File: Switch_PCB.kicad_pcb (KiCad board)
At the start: 2 copper layers, 213 x 96.6 mm, 75 parts, among them J1 Black, J10 Black, J11 Red, J12 Conn_01x02, J13 Conn_01x03, J14 Conn_01x03, J15 Conn_01x03, J16 Conn_01x03, J17 Jack 2.1mm, J18 Jack 2.1mm, J19 Black, J2 Red, J20 Red, J21 Black, J22 Red, J23 Black, J24 Red, J25 Black, J26 Red, J27 Black, J28 Red, J29 Black, J3 Black, J30 Red, J31 Black, J32 Red, J33 Black, J34 Red, J4 Red, J5 Black, J6 Red, J7 Black, J8 Red, J9 Red, SW1 Switch On-Off-On, SW2 Switch On-Off-On, SW3 Switch On-Off-On, SW4 Switch On-Off-On

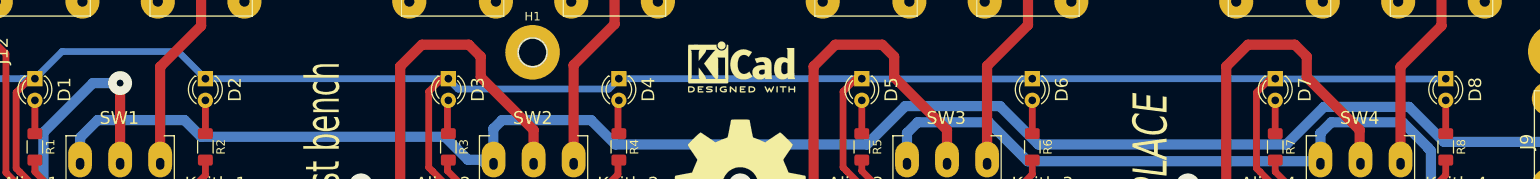
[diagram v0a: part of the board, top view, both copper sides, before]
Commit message: Change LED 3mm with 15.2mm Leads for 18 mm high * LED_D3.0mm_H18.0mm_Red * LED_D3.0mm_H18.0mm_Green
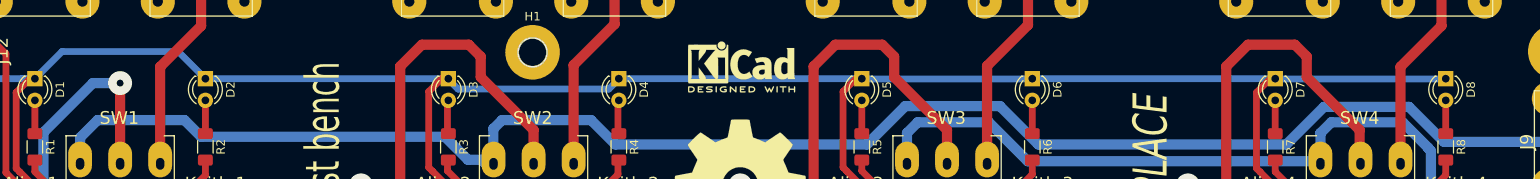
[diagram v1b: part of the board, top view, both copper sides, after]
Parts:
- D1, D3, D5, D7: footprint LED_THT:LED_D3.0mm -> Local_LED_THT:LED_D3.0mm_H18.0mm_Red
- D2, D4, D6, D8: footprint LED_THT:LED_D3.0mm -> Local_LED_THT:LED_D3.0mm_H18.0mm_Green

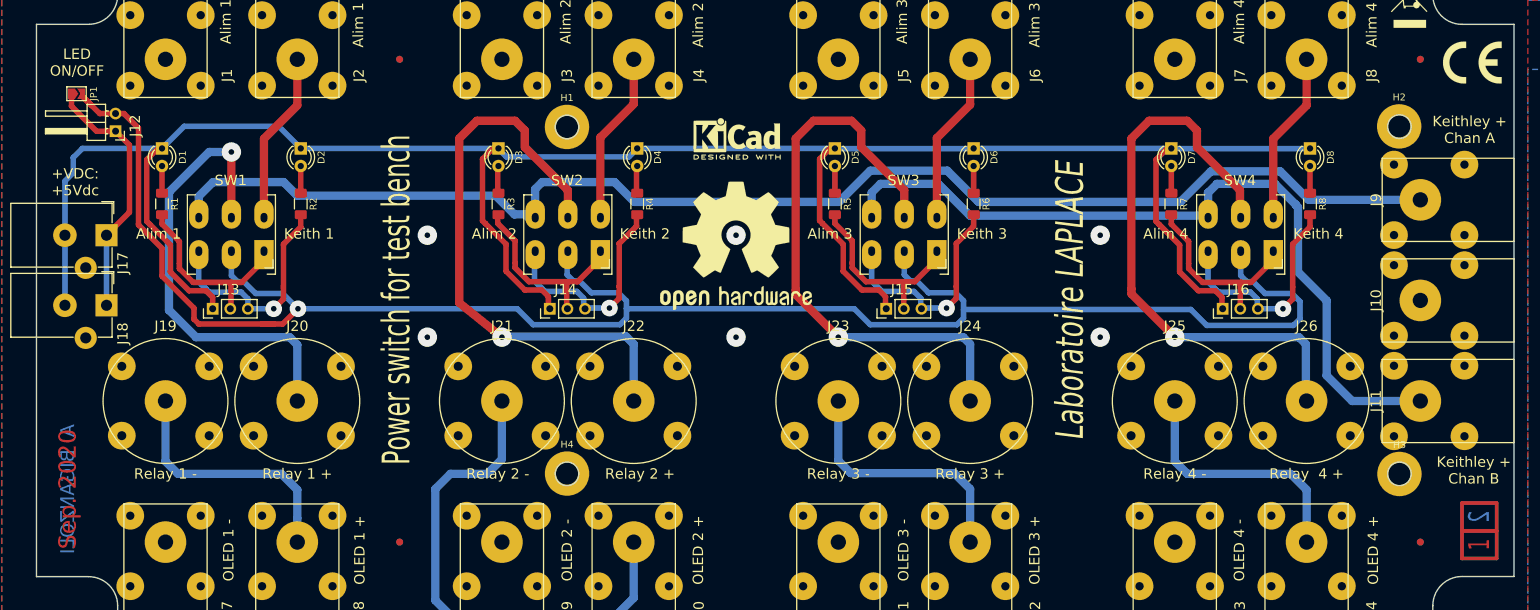
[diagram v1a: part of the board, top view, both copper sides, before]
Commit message: Update mechanical integration
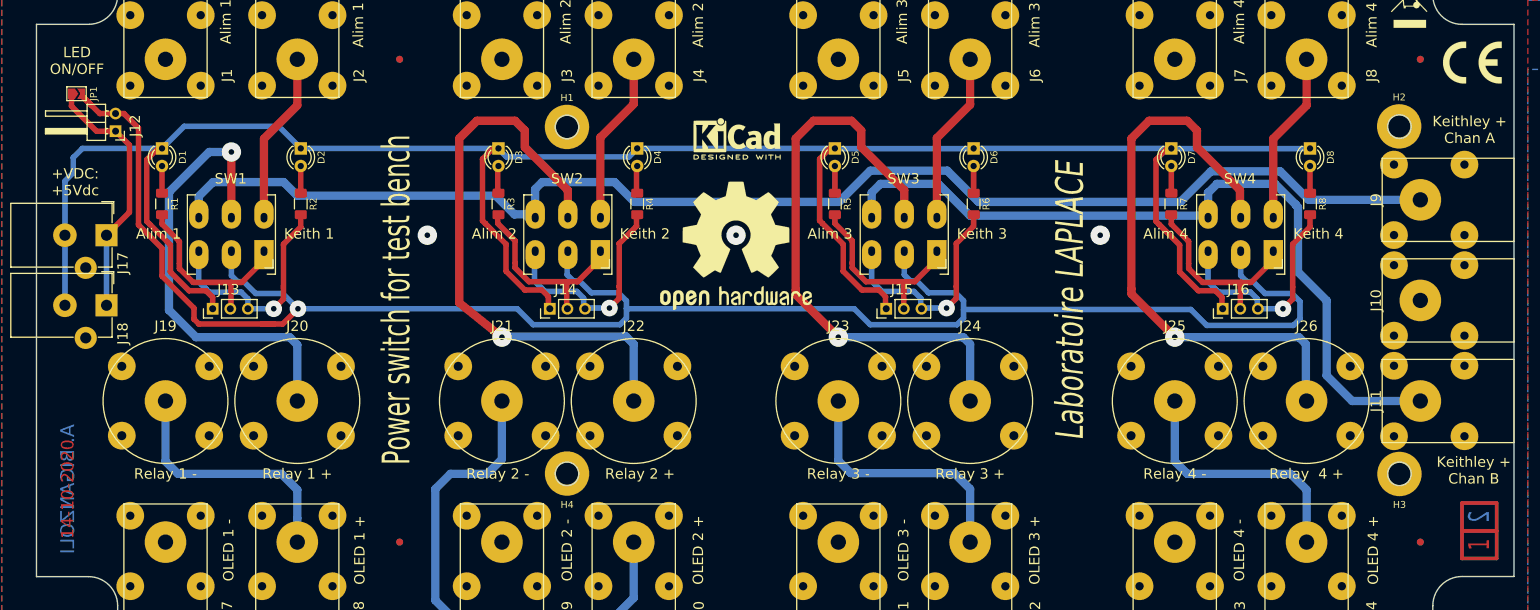
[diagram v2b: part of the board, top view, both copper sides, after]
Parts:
- JP1: value SolderJumper_2_Open -> SolderJumper
- turned Ref** to 90 degrees
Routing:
- net GNDPWR: vias 6 -> 3
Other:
- board text added: "14-10-2020"
- board text removed: "Sep. 2020"
